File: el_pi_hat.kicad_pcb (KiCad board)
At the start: 2 copper layers, 65 x 56 mm, 82 parts, among them J1 12V, J2 UART, J3 Raspberry Pi Header, J4 TRX, J5 MIC, J6 LINE OUT, J7 LINE IN, J8 HP OUT, Q1 2N7002, Q2 2N7002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

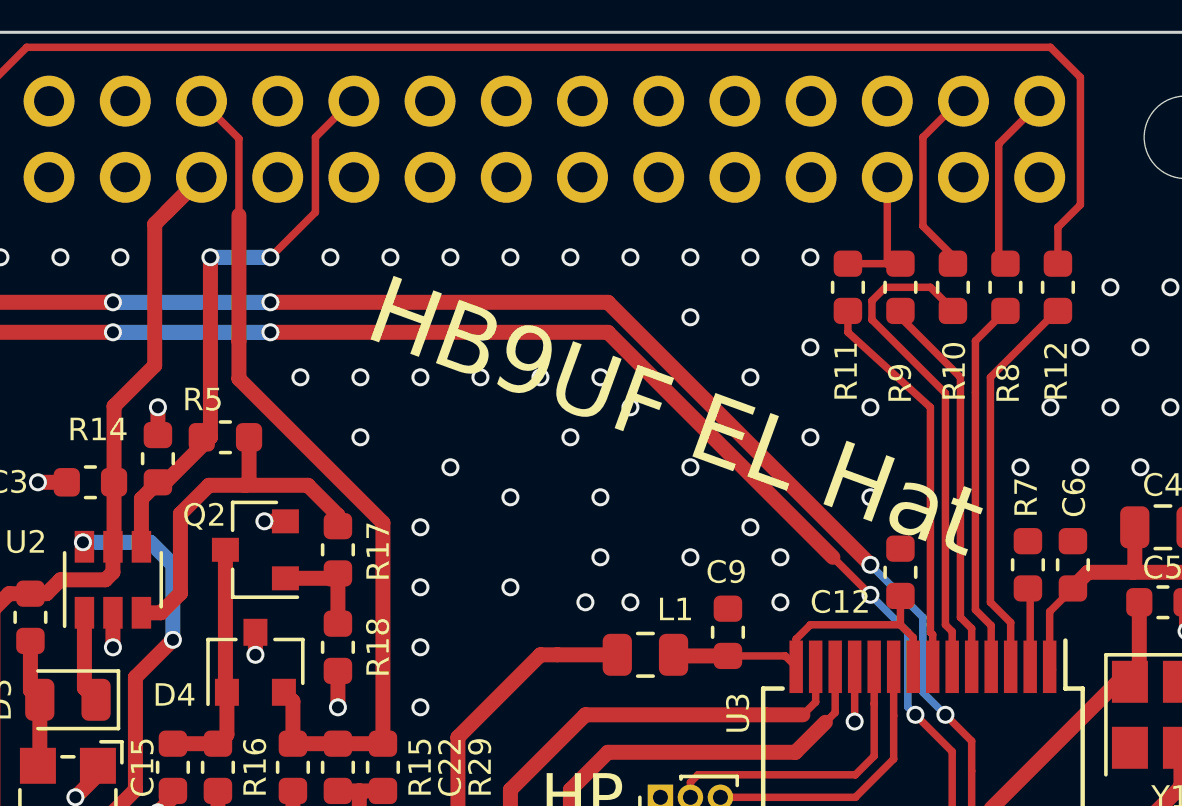
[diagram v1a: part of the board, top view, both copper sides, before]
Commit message: Improving Silk Screen text "HB9UF EL Hat". Fixes #7.
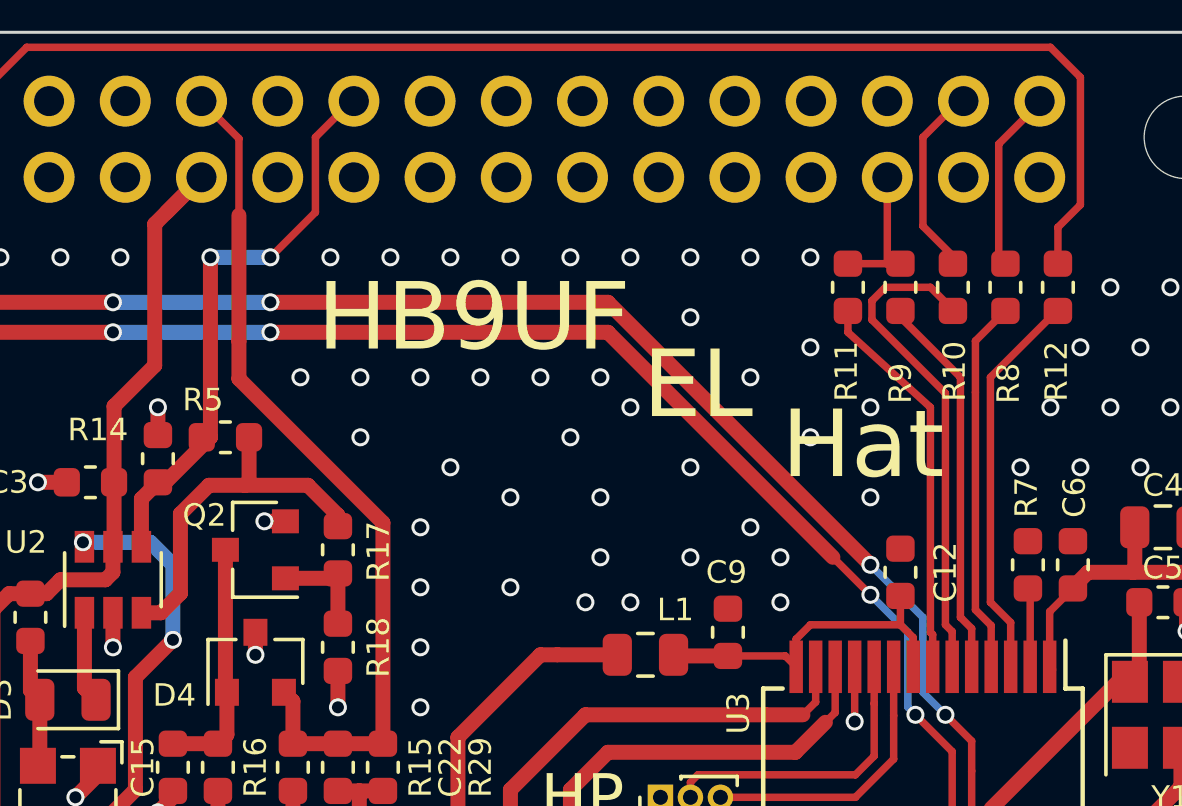
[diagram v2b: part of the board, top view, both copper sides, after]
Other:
- board text added: "EL"
- board text added: "HB9UF"
- board text added: "Hat"
- board text removed: "HB9UF EL Hat"

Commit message: Bumping Rev. from 1.0 to 1.1 in schematic and PCB
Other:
- board text added: "Rev 1.1, (c) 2020"
- board text removed: "Rev 1.0, (c) 2020"
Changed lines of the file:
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@@
   (page A4)
   (title_block
-    (rev 1.0)
+    (rev 1.1)
   )
   (layers
@@
     (34 B.Paste user)
     (35 F.Paste user)
-    (36 B.SilkS user hide)
+    (36 B.SilkS user)
     (37 F.SilkS user)
     (38 B.Mask user)
@@
     (effects (font (size 1.5 1.5) (thickness 0.3)) (justify left mirror))
   )
-  (gr_text "Rev 1.0, (c) 2020" (at 92.6 42.8) (layer B.SilkS)
+  (gr_text "Rev 1.1, (c) 2020" (at 92.6 42.8) (layer B.SilkS)
     (effects (font (size 1.5 1.5) (thickness 0.3)) (justify left mirror))
   )
